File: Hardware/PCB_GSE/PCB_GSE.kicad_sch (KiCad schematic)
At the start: 31 parts, among them J1 Conn_01x06_Pin, U1 STM32F103CBT6

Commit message: wip : Reduce BOM and fill all datasheet, digikey and MPN
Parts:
- C1, C4, C6, C8, C9: footprint Capacitor_SMD:C_0805_2012Metric -> Capacitor_SMD:C_0603_1608Metric; DigiKey_Part_Number (none) -> 399-C0603C104K3RACTUCT-ND; Manufacturer_Part_Number (none) -> C0603C104K3RACTU
- C2, C3: DigiKey_Part_Number (none) -> 1276-2891-1-ND; Manufacturer_Part_Number (none) -> CL21A106KAYNNNE
- C5, C7: footprint Capacitor_SMD:C_0603_1608Metric -> Capacitor_SMD:C_0805_2012Metric; DigiKey_Part_Number (none) -> 1276-2434-1-ND; Manufacturer_Part_Number (none) -> CL21B103KAANNNC
- FB1: DigiKey_Part_Number (none) -> 1934-1472-1-ND; Manufacturer_Part_Number (none) -> 2508051217Y6
- H1, H2, H3, H4, JP1, TP1, TP15, TP16, TP2: DigiKey_Part_Number (none) -> -
- J1: DigiKey_Part_Number (none) -> 732-5319-ND; Manufacturer_Part_Number (none) -> 61300611121
- LED1: footprint LTSTE683RGBW -> pcb_moteur:LTSTE683RGBW; DigiKey_Part_Number (none) -> 160-2215-1-ND
- R1, R2: DigiKey_Part_Number (none) -> 541-100CCT-ND; Manufacturer_Part_Number (none) -> CRCW0805100RFKEA
- R3, R9: footprint Resistor_SMD:R_0603_1608Metric -> Resistor_SMD:R_0805_2012Metric; DigiKey_Part_Number (none) -> 311-10.0KHRCT-ND; Manufacturer_Part_Number (none) -> RC0603FR-0710KL
- R4, R5, R6, R7: DigiKey_Part_Number (none) -> RHM22DCT-ND; Manufacturer_Part_Number (none) -> ESR03EZPJ220
- R8: footprint Resistor_SMD:R_0603_1608Metric -> Resistor_SMD:R_0805_2012Metric; DigiKey_Part_Number (none) -> P1.5KDBCT-ND; Manufacturer_Part_Number (none) -> ERA-3AEB152V
- U1: DigiKey_Part_Number (none) -> 497-6288-ND; Manufacturer_Part_Number (none) -> STM32F103CBT6

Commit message: wip: begining layout
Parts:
- added R6: 22R, Resistor_SMD:R_0603_1608Metric, symbol Device:R_Small
- renumbered R9 to R10, R6 to R7, R7 to R8, R8 to R9, TP15 to TP3, TP16 to TP4
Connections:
- net ISO_CAN_OUT: now also R6.1; no longer U1.2 (PC13)
- new net: R6.2, U1.2 (PC13)
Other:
- moved on the sheet: C1, R3

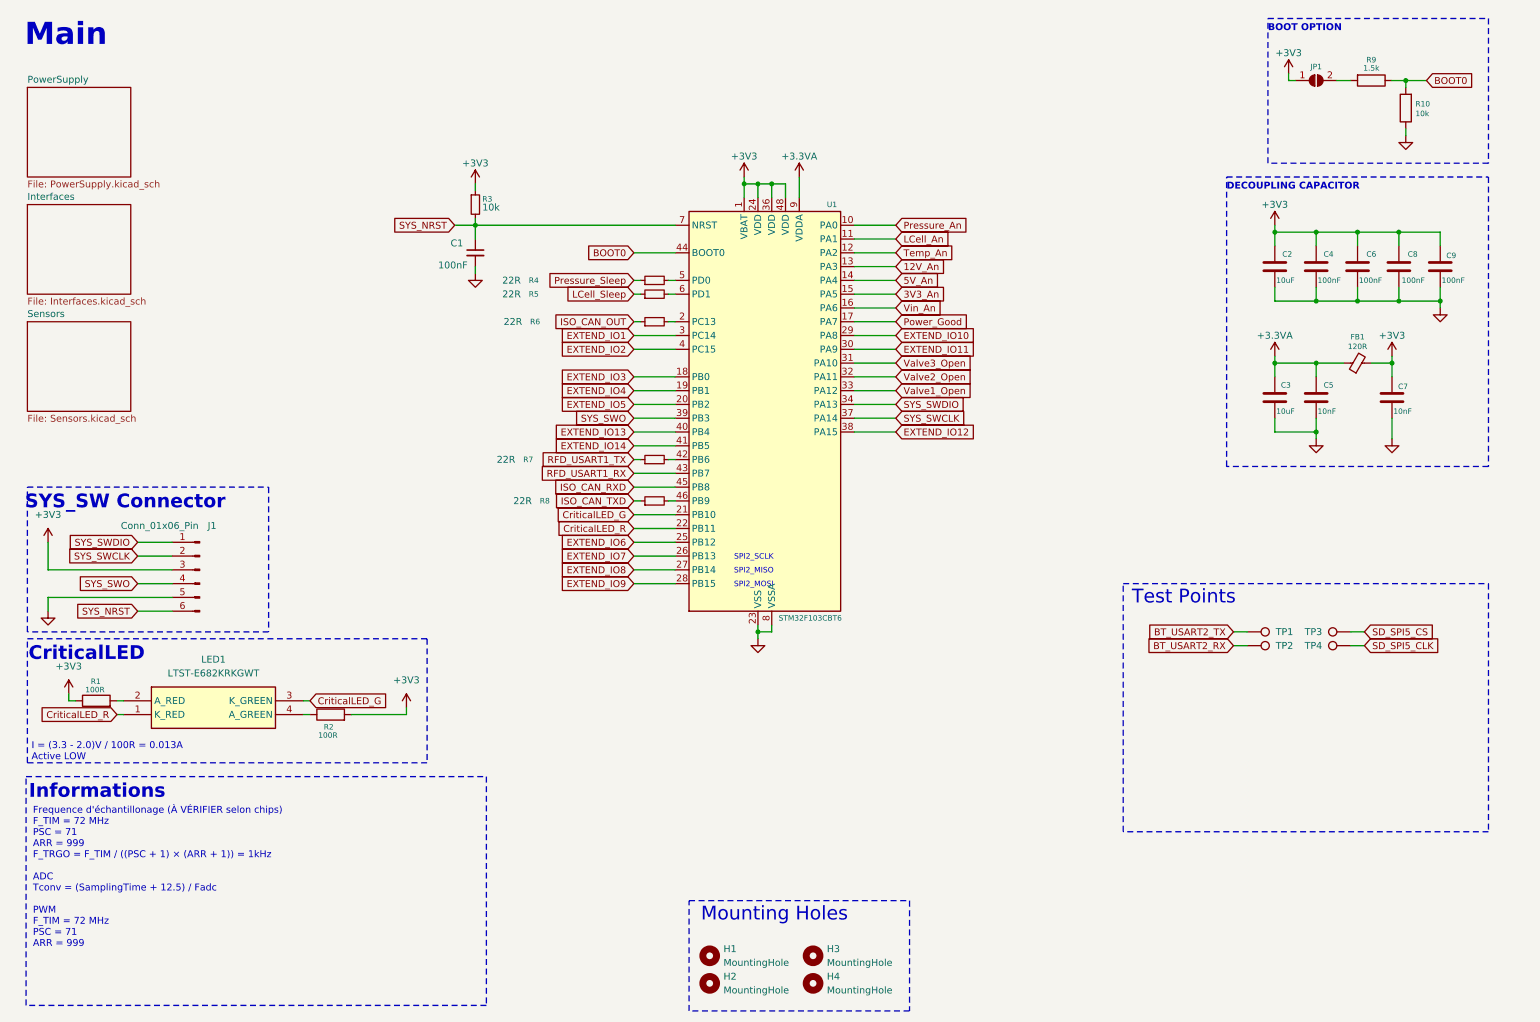
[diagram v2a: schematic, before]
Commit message: feat: add 8MHz crystal, fix extended ios, fix pinout with HSE, update smt32 project, begin layout edge
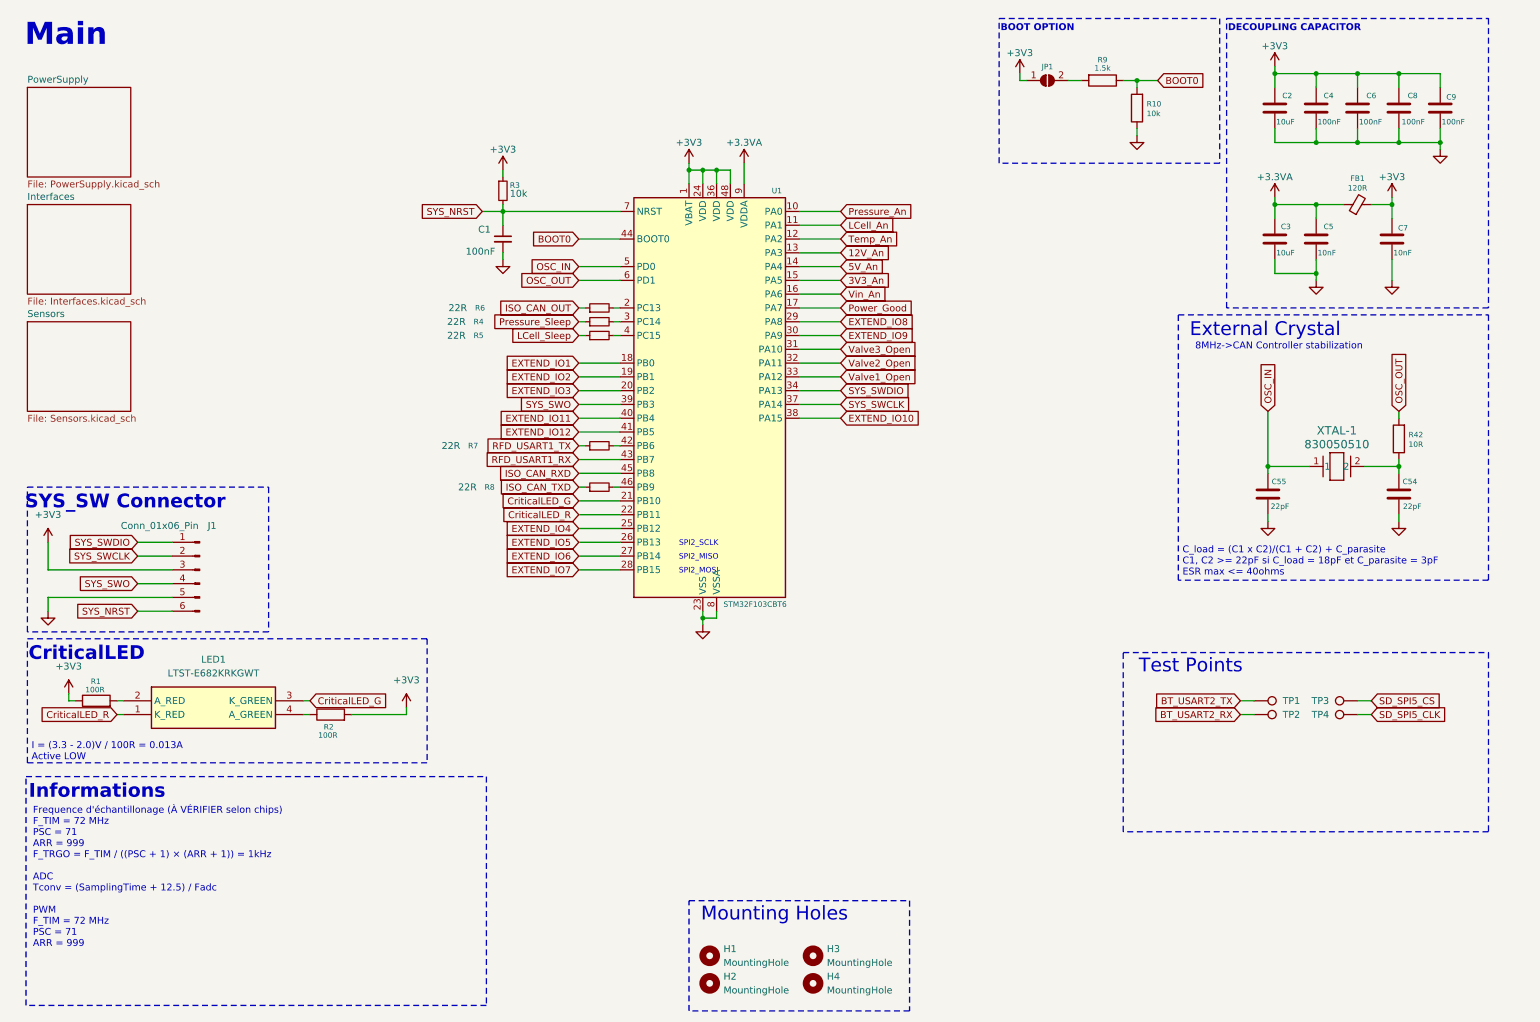
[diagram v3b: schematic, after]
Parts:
- added C54, C55: 22pF, Capacitor_SMD:C_0805_2012Metric, symbol Device:C
- added R42: 10R, Resistor_SMD:R_0805_2012Metric, symbol Device:R
- added XTAL-1: 830050510, PCB_GSE:830050510, symbol PCB_GSE:830050510
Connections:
- net EXTEND_IO13 is gone; now on net EXTEND_IO11: U1.40 (PB4)
- net EXTEND_IO14 is gone; now on net EXTEND_IO12: U1.41 (PB5)
- net EXTEND_IO1: now also U1.18 (PB0); no longer U1.3 (PC14)
- net EXTEND_IO10: now also U1.38 (PA15); no longer U1.29 (PA8)
- net EXTEND_IO11: no longer U1.30 (PA9)
- net EXTEND_IO12: no longer U1.38 (PA15)
- net EXTEND_IO2: now also U1.19 (PB1); no longer U1.4 (PC15)
- net EXTEND_IO3: now also U1.20 (PB2); no longer U1.18 (PB0)
- net EXTEND_IO4: now also U1.25 (PB12); no longer U1.19 (PB1)
- net EXTEND_IO5: now also U1.26 (PB13); no longer U1.20 (PB2)
- net EXTEND_IO6: now also U1.27 (PB14); no longer U1.25 (PB12)
- net EXTEND_IO7: now also U1.28 (PB15); no longer U1.26 (PB13)
- net EXTEND_IO8: now also U1.29 (PA8); no longer U1.27 (PB14)
- net EXTEND_IO9: now also U1.30 (PA9); no longer U1.28 (PB15)
- net GND: now also C54.1, C55.1
- net at R4.2: now also U1.3 (PC14); no longer U1.5 (PD0)
- net at R5.2: now also U1.4 (PC15); no longer U1.6 (PD1)
- new net: C54.2, R42.1, XTAL-1.2
- new net OSC_IN: C55.2, U1.5 (PD0), XTAL-1.1
- new net OSC_OUT: R42.2, U1.6 (PD1)
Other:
- note added: "8MHz->CAN Controller stabilization"
- note added: "C_load = (C1 x C2)/(C1 + C2) + C_parasite C1, C2 >= 22pF si C_load = 18pF et C_parasite = 3pF ESR max <= 40ohms"
- note added: "External Crystal"
- moved on the sheet: C1, C2, C3, C4, C5, C6, C7, C8, C9, FB1, JP1, R10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

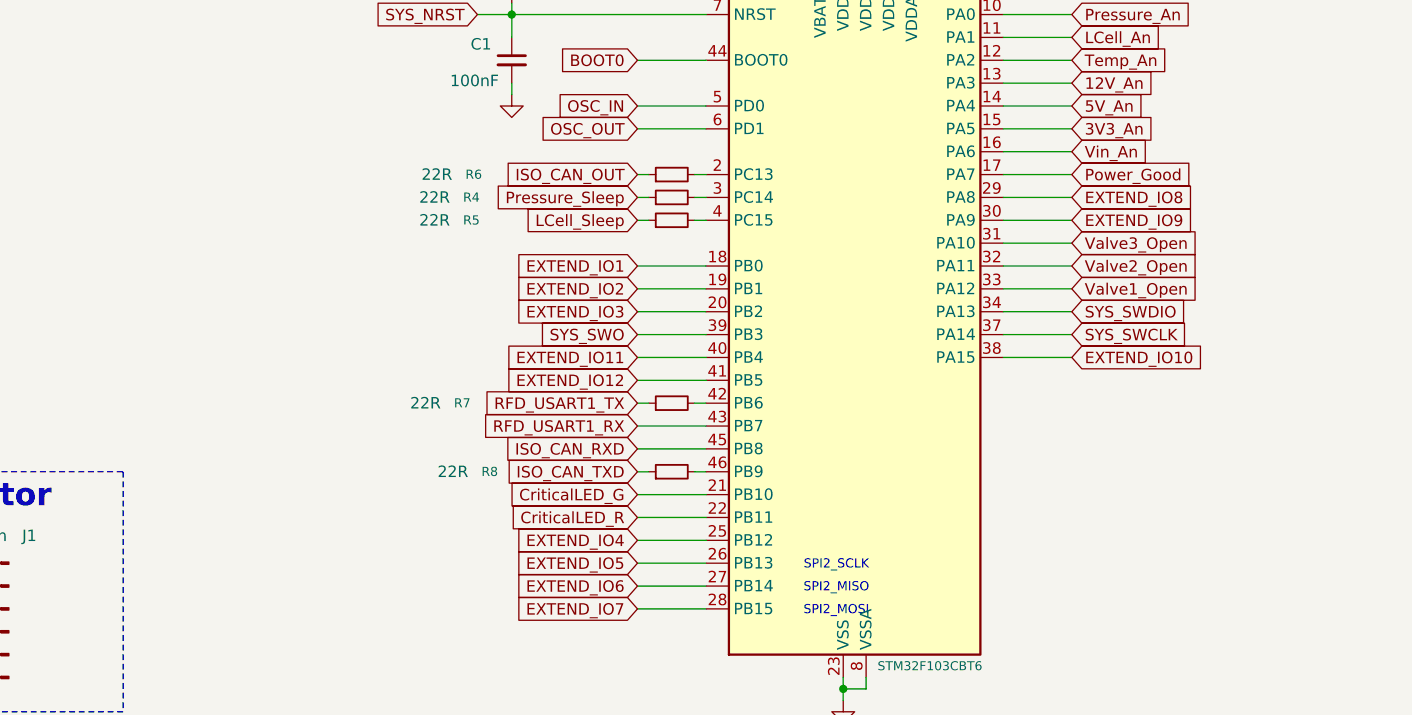
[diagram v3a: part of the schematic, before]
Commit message: change 12V buck to 12V buck-boost
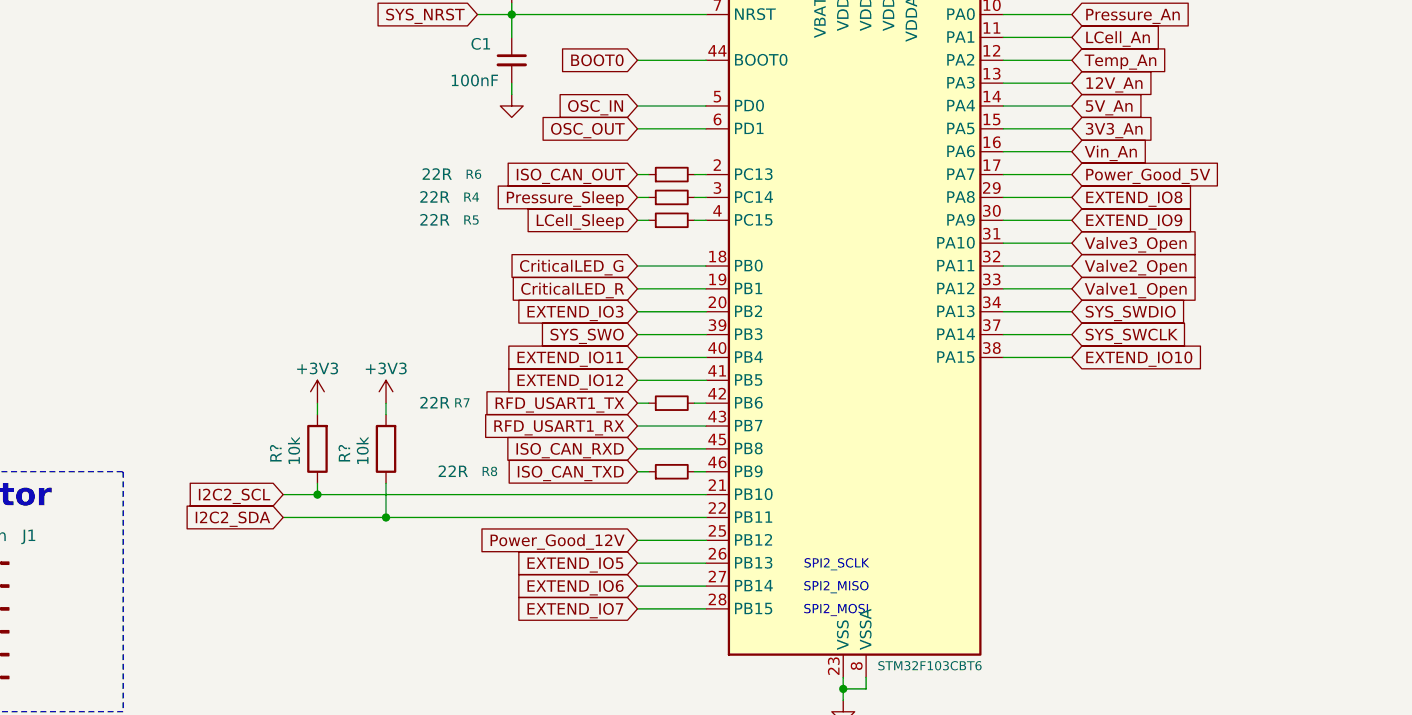
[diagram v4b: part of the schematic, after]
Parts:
- added R? (x2): 10k, Resistor_SMD:R_0805_2012Metric, symbol Device:R
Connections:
- net EXTEND_IO1 is gone; now on net CriticalLED_G: U1.18 (PB0)
- net EXTEND_IO2 is gone; now on net CriticalLED_R: U1.19 (PB1)
- net +3V3: now also R?.2, R?.2
- net CriticalLED_G: no longer U1.21 (PB10)
- net CriticalLED_R: no longer U1.22 (PB11)
- net EXTEND_IO4 renamed Power_Good_12V
- net Power_Good renamed Power_Good_5V
- new net I2C2_SCL: R?.1, U1.21 (PB10)
- new net I2C2_SDA: R?.1, U1.22 (PB11)

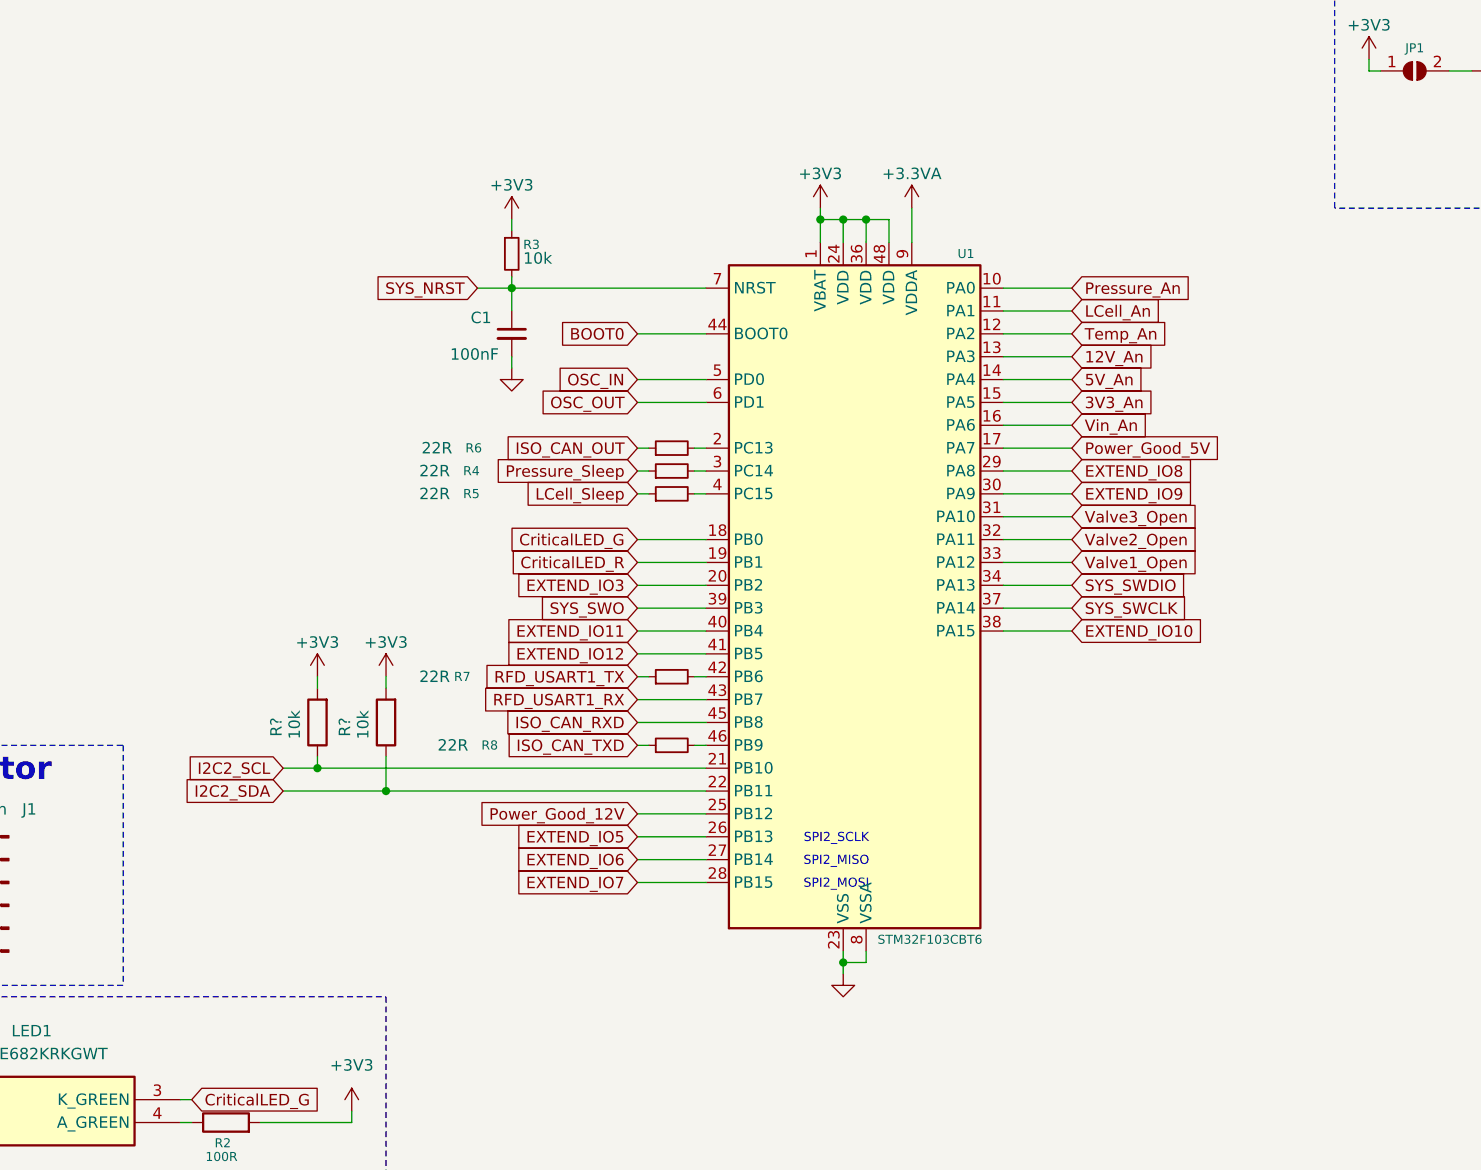
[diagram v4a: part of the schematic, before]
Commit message: wip : add BOM for 12V buck-boost
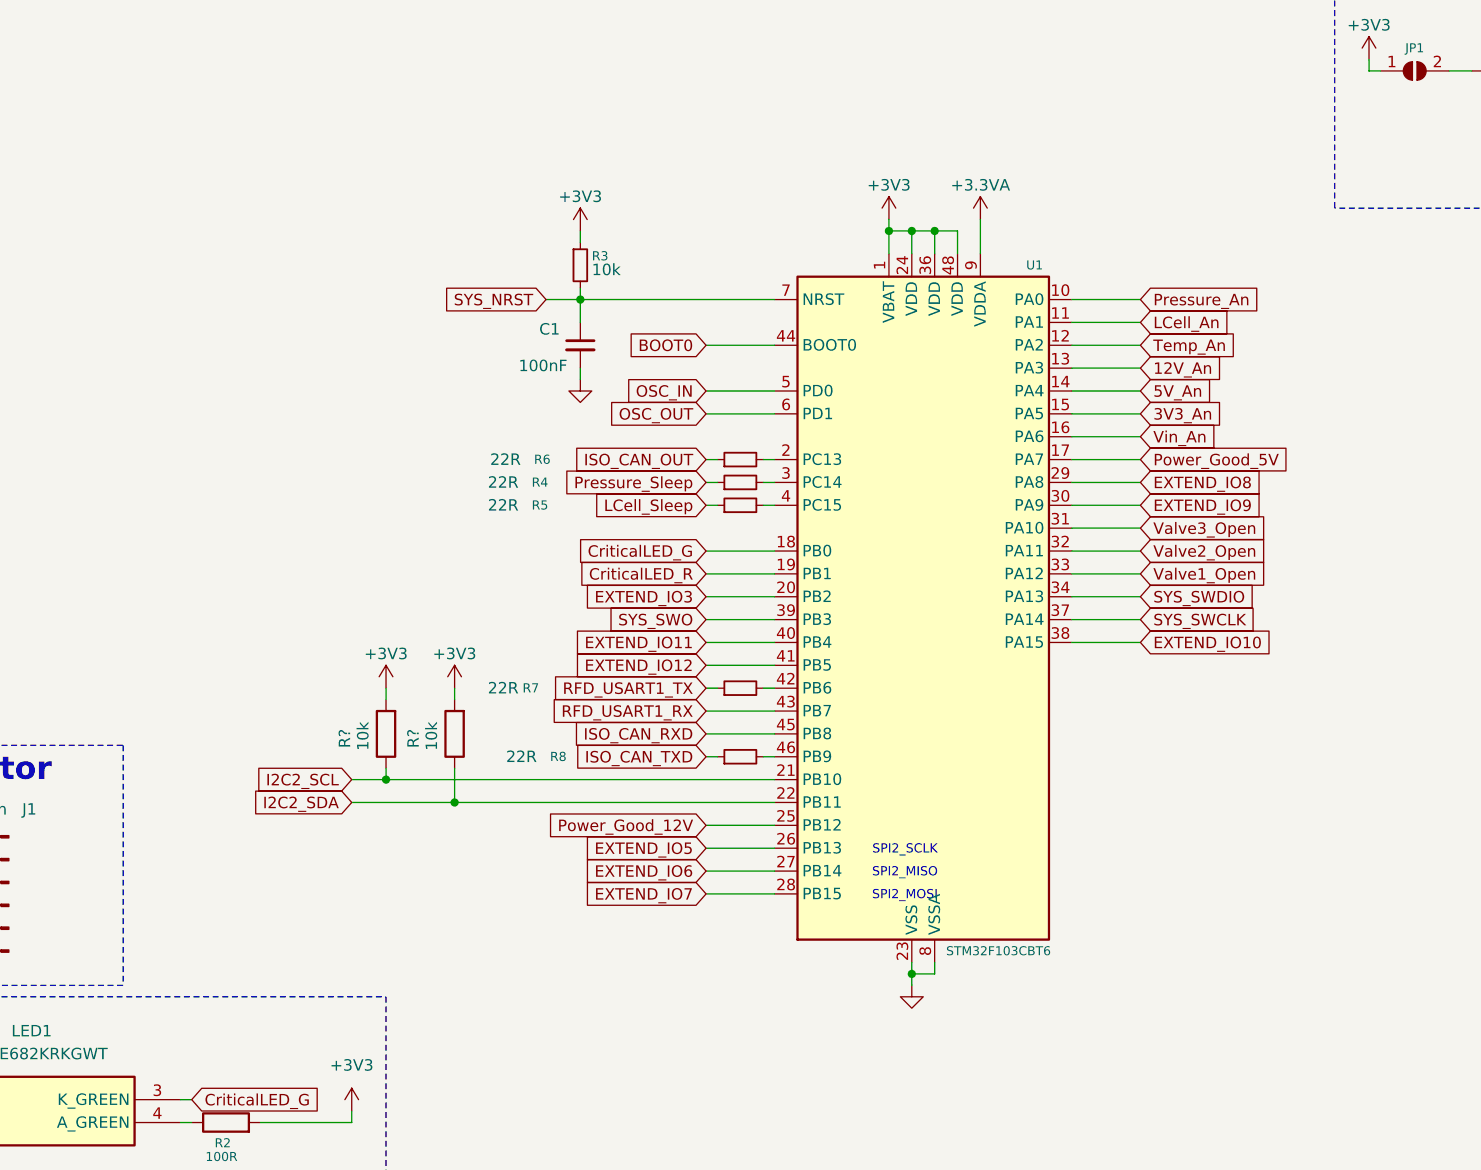
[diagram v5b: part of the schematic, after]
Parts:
- XTAL-1: DigiKey_Part_Number (none) -> 1923-830050510CT-ND; Manufacturer_Part_Number (none) -> 830050510
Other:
- moved on the sheet: C1, R3, R4, R5, R6, R7, R8, R?, U1

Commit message: wip : subsystems layout
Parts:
- gave numbers to parts that had none: 2
- renumbered C54 to C10, C9 to C11, C55 to C2, C2 to C3, C3 to C4, C4 to C5, C5 to C6, C6 to C7, C7 to C8, C8 to C9, R8 to R10, R9 to R11, R10 to R12, R42 to R13, R3 to R5, R4 to R7, R5 to R8, R7 to R9
